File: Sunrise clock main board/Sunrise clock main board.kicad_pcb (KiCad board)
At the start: 2 copper layers, 160 x 106.7 mm, 133 parts, among them J1 Barrel_Jack_Switch, J3 Screw terminal/dnf, J4 Conn_02x05_Odd_Even, J5 Conn_01x04_Male, J6 Conn_01x04_Male, Q1 IRML2244, Q2 IRML2244, Q3 2N7002, Q4 2N7002, SW1 SW_Push, SW2 SW_Push, SW3 SW_Push, SW4 SW_Push, SW5 SW_Push, SW6 SW_Push, SW7 SW_Push, SW8 SW_Push, U1 NCP1117LPST33T3G, U10 74HC138D, U11 INA219AIDCNR, U2 MAX809S, U3 LM358DR, U4 DS3231MZ, U5 AT24C512C-SSHD, U6 PCA9306DCTR, U7 74AHCT125D, U8 74HC4066D, U9 MCP23017_SP

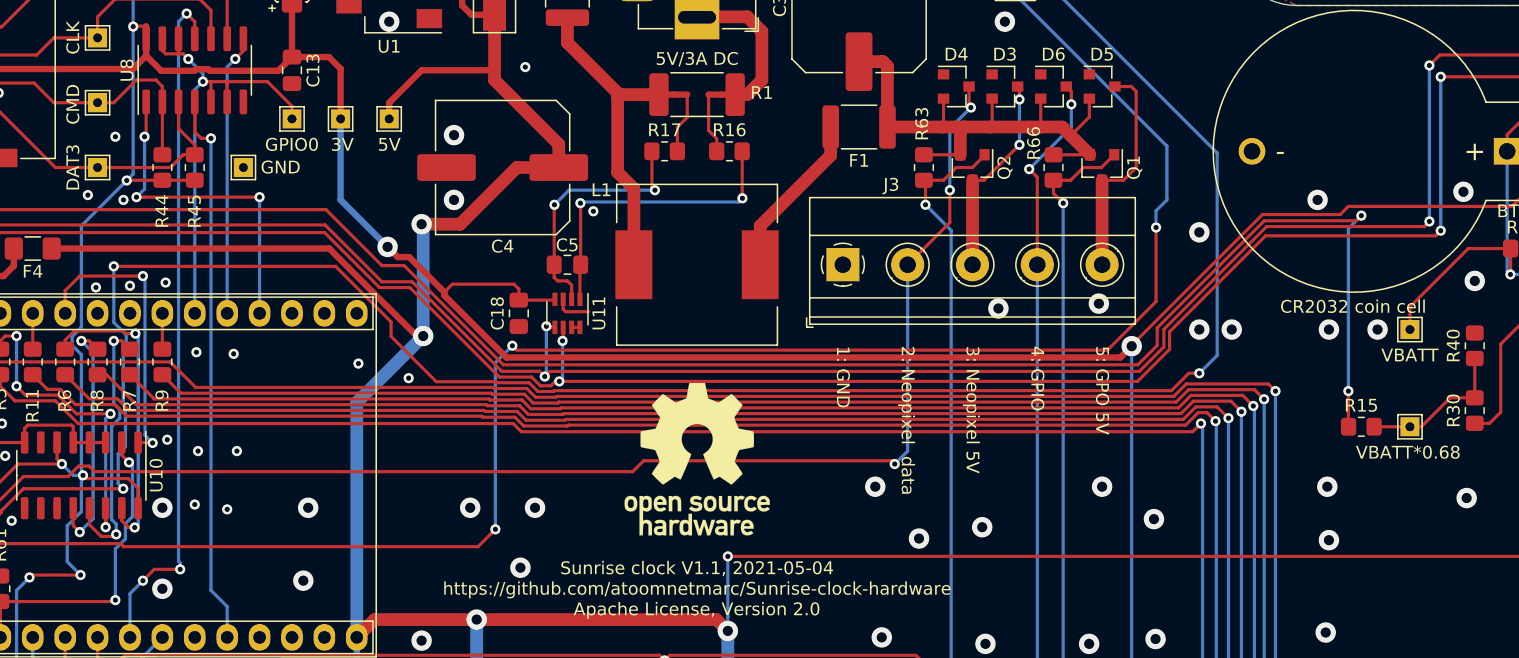
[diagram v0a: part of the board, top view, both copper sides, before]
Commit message: Changed INA219AxDCN to INA219AxD
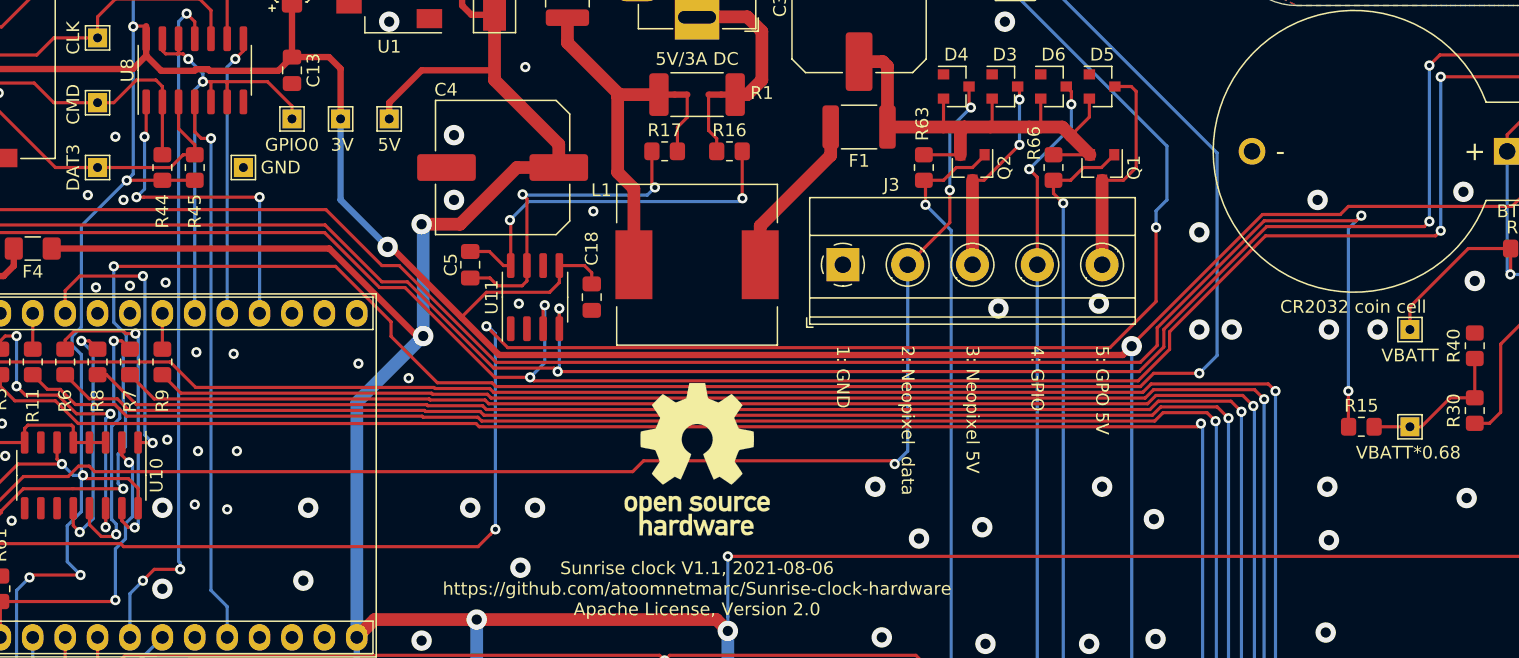
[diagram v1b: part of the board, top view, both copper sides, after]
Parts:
- U11: value INA219AIDCNR -> INA219AxD; footprint Package_TO_SOT_SMD:SOT-23-8 -> Package_SO:SOIC-8_3.9x4.9mm_P1.27mm
- moved C5 7.62 mm to (-17.8, -25.4), turned to 270 degrees
- moved C18 5.85 mm to (-8.26, -22.9)
- moved U11 2.84 mm to (-12.7, -22.9), turned to 90 degrees
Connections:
- U11 pad 1: Net-(C5-Pad1) -> GND
- U11 pad 2: Net-(C5-Pad2) -> GND
- U11 pad 3: GND -> SDA_3V
- U11 pad 4: +3V3 -> SCL_3V
- U11 pad 5: SCL_3V -> +3V3
- U11 pad 6: SDA_3V -> GND
- U11 pad 7: GND -> Net-(C5-Pad2)
- U11 pad 8: GND -> Net-(C5-Pad1)
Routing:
- net Net-(C5-Pad1): track 24.1 -> 29.8 mm
- net Net-(C5-Pad2): track 19.9 -> 25.4 mm
- net 3V_MCU: track 175.8 -> 179.6 mm
- net +3V3: track 444.1 -> 447.5 mm
- net GND: track 66.3 -> 62.8 mm, vias 111 -> 112
- net SDA_3V: track 244.0 -> 247.3 mm
- net SCL_3V: track 243.6 -> 245.1 mm
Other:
- board text added: "Sunrise clock V1.1, 2021-08-06 https://github.com/atoomnetmarc/Sunrise-clock-hardware Apache License, Version 2.0"
- board text removed: "Sunrise clock V1.1, 2021-05-04 https://github.com/atoomnetmarc/Sunrise-clock-hardware Apache License, Version 2.0"

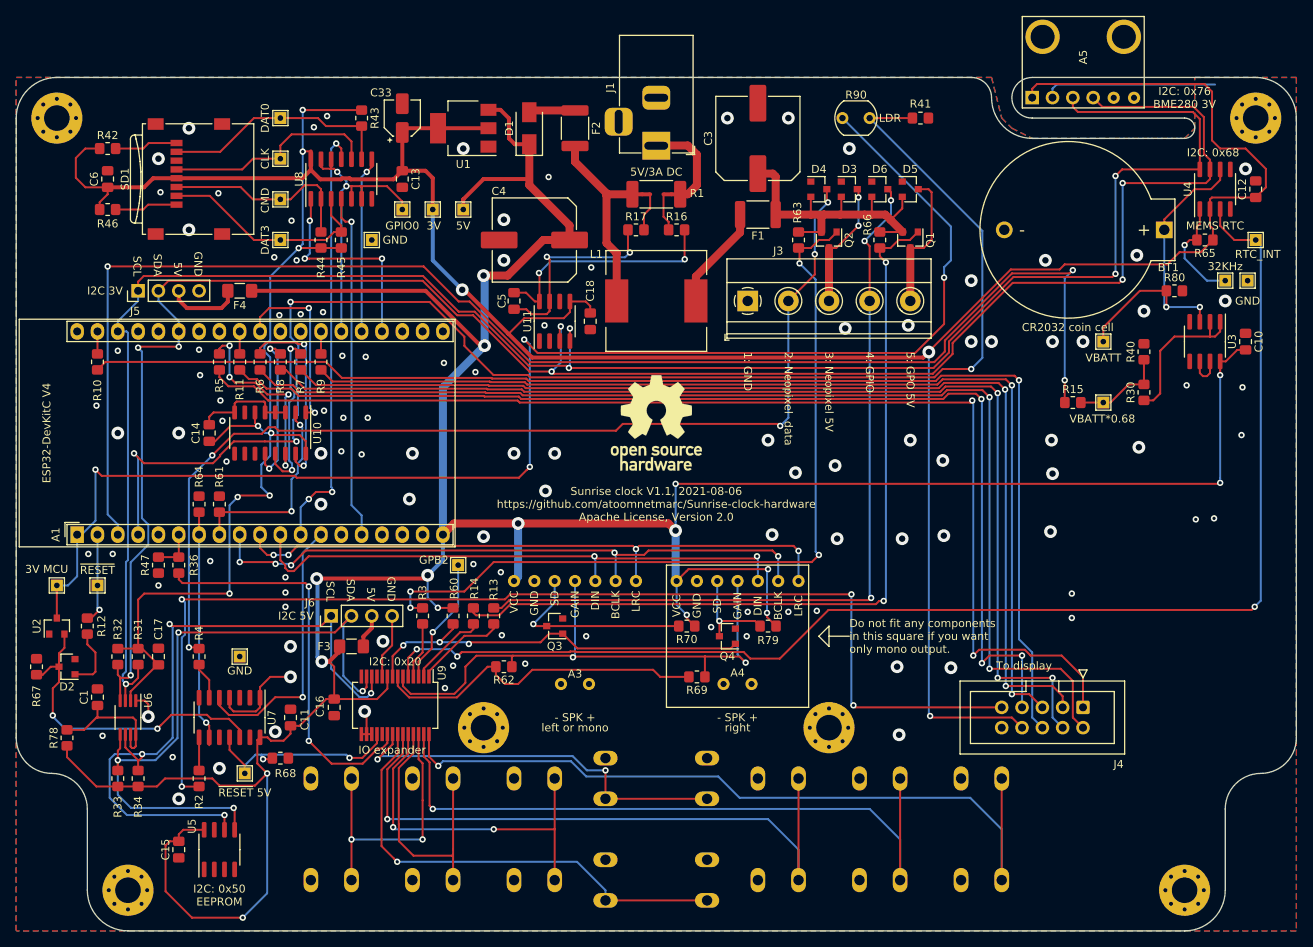
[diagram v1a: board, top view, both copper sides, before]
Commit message: Update to Kicad 6.
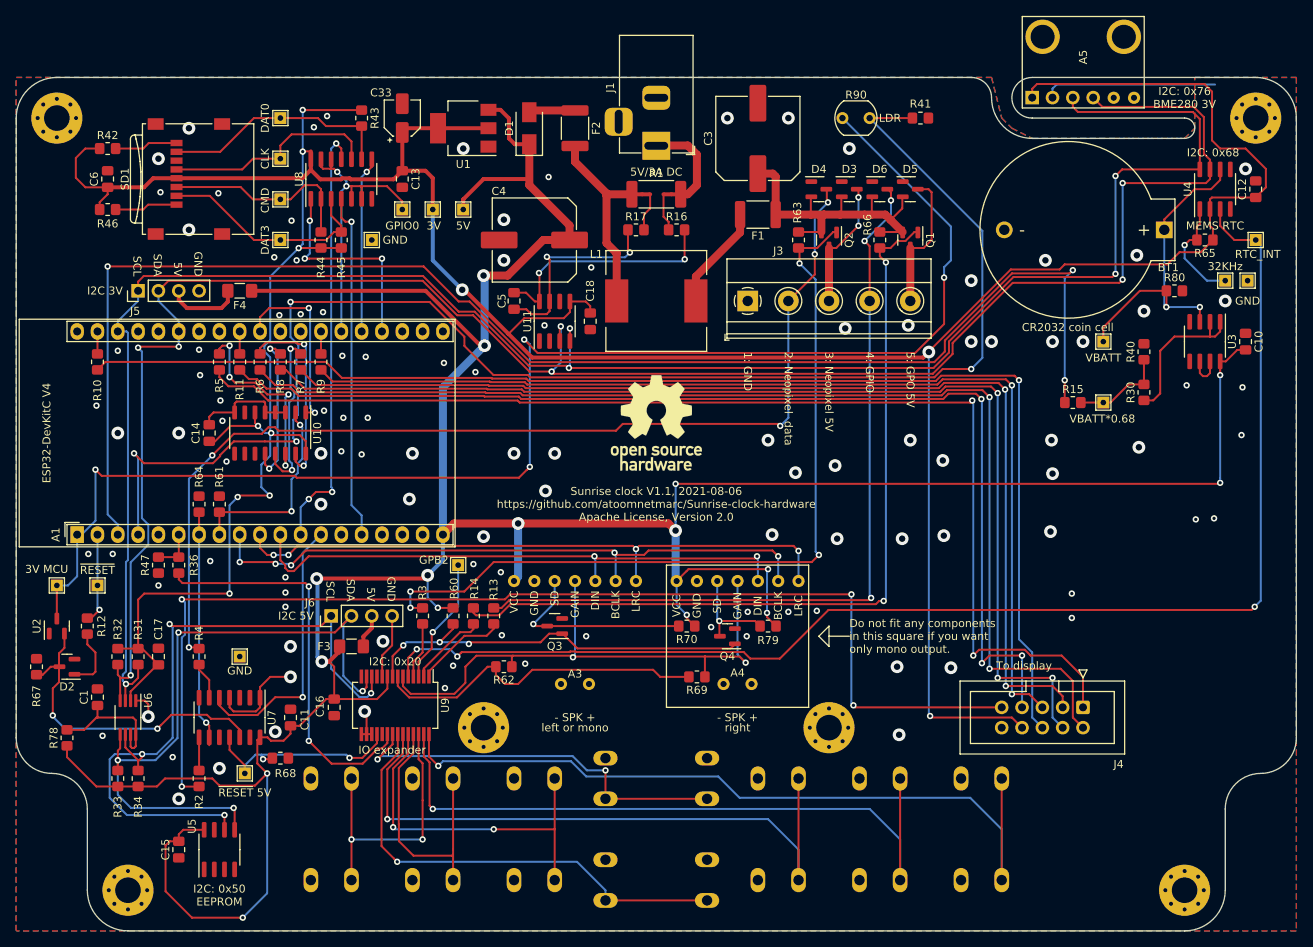
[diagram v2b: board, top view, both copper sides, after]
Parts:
- R1: footprint Resistor_SMD:R_2512_6332Metric_Pad1.52x3.35mm_HandSolder -> Resistor_SMD:R_2512_6332Metric_Pad1.40x3.35mm_HandSolder
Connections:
- net LCD1_~CE renamed LCD1_~{CE}
- net LCD2_~CE renamed LCD2_~{CE}
- net LCD3_~CE renamed LCD3_~{CE}
- net LCD_DATA-~CMD renamed LCD_DATA-~{CMD}
- net LCD_~RST renamed LCD_~{RST}
- net NEOPIXEL_~EN renamed NEOPIXEL_~{EN}
- net ~RESET renamed ~{RESET}
- net ~RESET_5V renamed ~{RESET_5V}
- net ~SDL renamed ~{SDL}
- net ~SDR renamed ~{SDR}
- A1 pad 16: Net-(A1-Pad16) -> unconnected-(A1-Pad16)
- A1 pad 17: Net-(A1-Pad17) -> unconnected-(A1-Pad17)
- A1 pad 18: Net-(A1-Pad18) -> unconnected-(A1-Pad18)
- A1 pad 20: Net-(A1-Pad20) -> unconnected-(A1-Pad20)
- A1 pad 21: Net-(A1-Pad21) -> unconnected-(A1-Pad21)
- A1 pad 22: Net-(A1-Pad22) -> unconnected-(A1-Pad22)
- A1 pad 27: Net-(A1-Pad27) -> unconnected-(A1-Pad27)
- A1 pad 28: Net-(A1-Pad28) -> unconnected-(A1-Pad28)
- A1 pad 31: Net-(A1-Pad31) -> unconnected-(A1-Pad31)
- A1 pad 34: Net-(A1-Pad34) -> unconnected-(A1-Pad34)
- A1 pad 35: Net-(A1-Pad35) -> unconnected-(A1-Pad35)
- A1 pad 5: Net-(A1-Pad5) -> unconnected-(A1-Pad5)
- A3 pad 8: Net-(A3-Pad8) -> unconnected-(A3-Pad8)
- A3 pad 9: Net-(A3-Pad9) -> unconnected-(A3-Pad9)
- A4 pad 8: Net-(A4-Pad8) -> unconnected-(A4-Pad8)
- A4 pad 9: Net-(A4-Pad9) -> unconnected-(A4-Pad9)
- A5 pad 5: Net-(A5-Pad5) -> unconnected-(A5-Pad5)
- A5 pad 6: Net-(A5-Pad6) -> unconnected-(A5-Pad6)
- D2 pad 2: Net-(D2-Pad2) -> unconnected-(D2-Pad2)
- U10 pad 10: Net-(U10-Pad10) -> unconnected-(U10-Pad10)
- U10 pad 11: Net-(U10-Pad11) -> unconnected-(U10-Pad11)
- U10 pad 7: Net-(U10-Pad7) -> unconnected-(U10-Pad7)
- U10 pad 9: Net-(U10-Pad9) -> unconnected-(U10-Pad9)
- U4 pad 4: Net-(U4-Pad4) -> unconnected-(U4-Pad4)
- U5 pad 1: Net-(U5-Pad1) -> unconnected-(U5-Pad1)
- U5 pad 2: Net-(U5-Pad2) -> unconnected-(U5-Pad2)
- U5 pad 3: Net-(U5-Pad3) -> unconnected-(U5-Pad3)
- U5 pad 7: Net-(U5-Pad7) -> unconnected-(U5-Pad7)
- U7 pad 3: Net-(U7-Pad3) -> unconnected-(U7-Pad3)
- U9 pad 11: Net-(U9-Pad11) -> unconnected-(U9-Pad11)
- U9 pad 14: Net-(U9-Pad14) -> unconnected-(U9-Pad14)
- U9 pad 19: Net-(U9-Pad19) -> unconnected-(U9-Pad19)
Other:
- net class Default removed
- board text added: "~{RESET}"
- board text added: "~{RESET} 5V"
- board text removed: "~RESET"
- board text removed: "~RESET 5V"
